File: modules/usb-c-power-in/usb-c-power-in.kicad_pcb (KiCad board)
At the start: 2 copper layers, 20.8 x 34.6 mm, 2 parts, among them J1 Conn_01x02

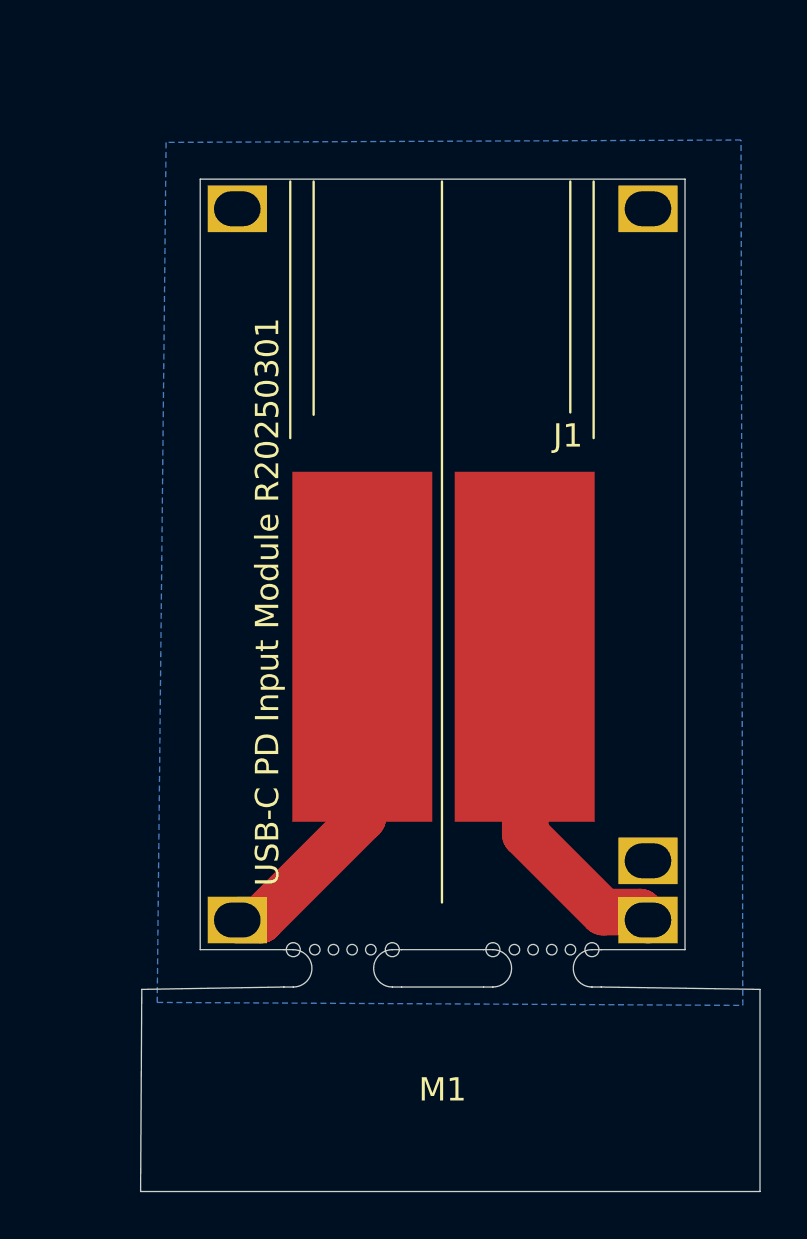
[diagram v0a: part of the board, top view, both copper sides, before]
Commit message: Updating USB-Power-IN
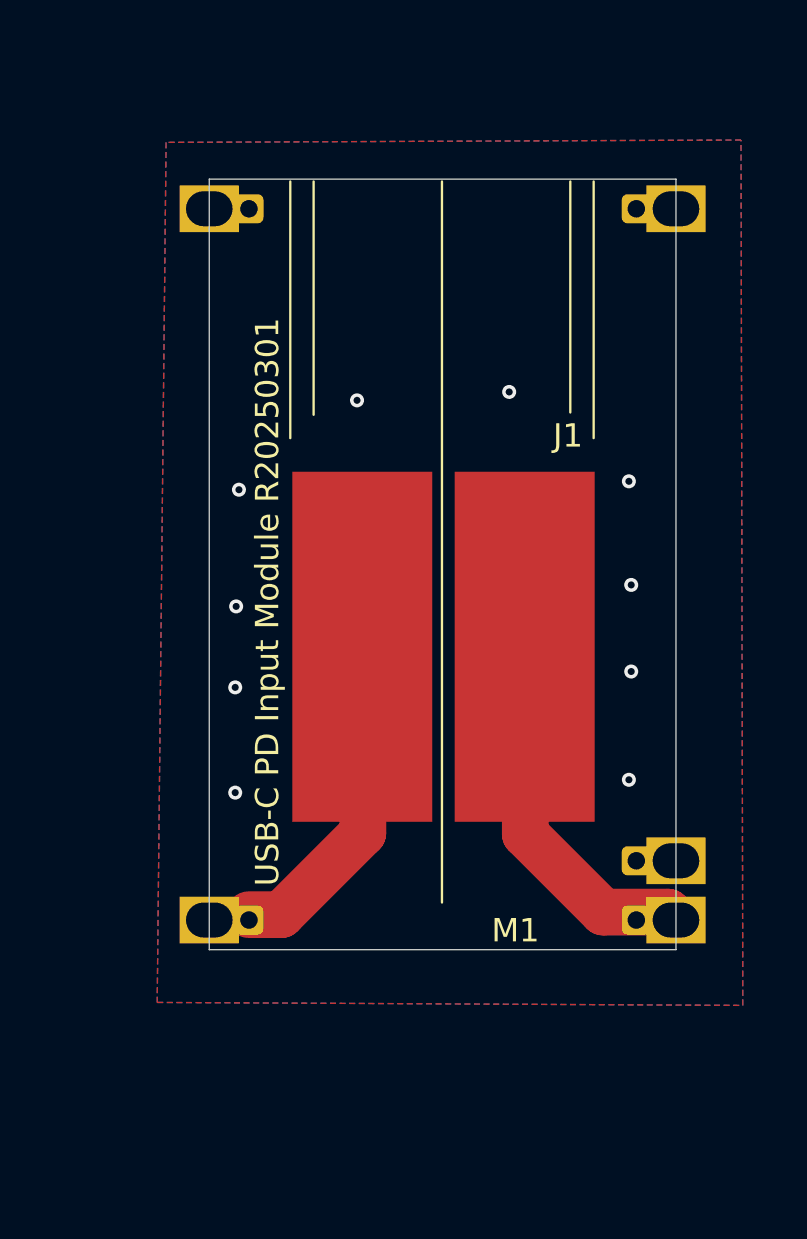
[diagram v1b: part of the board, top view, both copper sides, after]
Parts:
- M1: footprint MegaCastle:MegaCastle2x13-Module-I14.0x28.2-M800C00C-PANEL-NIBBLE -> MegaCastle:MegaCastle2x13-Module-I20.0x28.2-M800C00C-SPAREPAD
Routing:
- net +20V: track 13.7 -> 14.9 mm
- net GND: track 13.4 -> 13.2 mm, vias 0 -> 10
- added copper zone on F.Cu, net GND
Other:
- board size 20.8 x 34.6 mm -> 20 x 33 mm
